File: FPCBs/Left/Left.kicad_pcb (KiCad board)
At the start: 2 copper layers, 20.8 x 40 mm, 7 parts, among them J1 Conn_01x02_Pin, SW1 SW_Rotary_1x6_MP

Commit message: Add connector
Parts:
- J1: footprint Connector_Coaxial:WR-MMCX_Wuerth_66012102111404_Vertical -> Leica-G9ii:FPC-2Rows-27Pins-0.23mm
- moved J1 57.2 mm to (147.1, 93.6), turned to 90 degrees
- moved R5 12.0 mm to (102.6, 98.0), turned to -108 degrees
- moved R1 12.0 mm to (114.4, 98.1), turned to 108 degrees
- moved R4 7.50 mm to (104.8, 94.9), turned to -144 degrees
- moved R2 7.40 mm to (112.2, 94.9), turned to 144 degrees
- moved R3 0.13 mm to (108.5, 93.7), turned to 180 degrees
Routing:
- net Net-(J1-Pin_2): track 27.5 -> 68.5 mm
- net Net-(J1-Pin_1): track 33.0 -> 38.9 mm
- net Net-(R3-Pad2): track 4.93 -> 4.28 mm
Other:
- board size 20.8 x 40 mm -> 47.4 x 14.5 mm

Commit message: Update to kicad 9
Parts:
- J1: value Conn_01x02_Pin -> To PCB; footprint Leica-G9ii:FPC-2Rows-27Pins-0.23mm -> Leica-G9ii:FPC-2Rows-27Pins-0.5mm

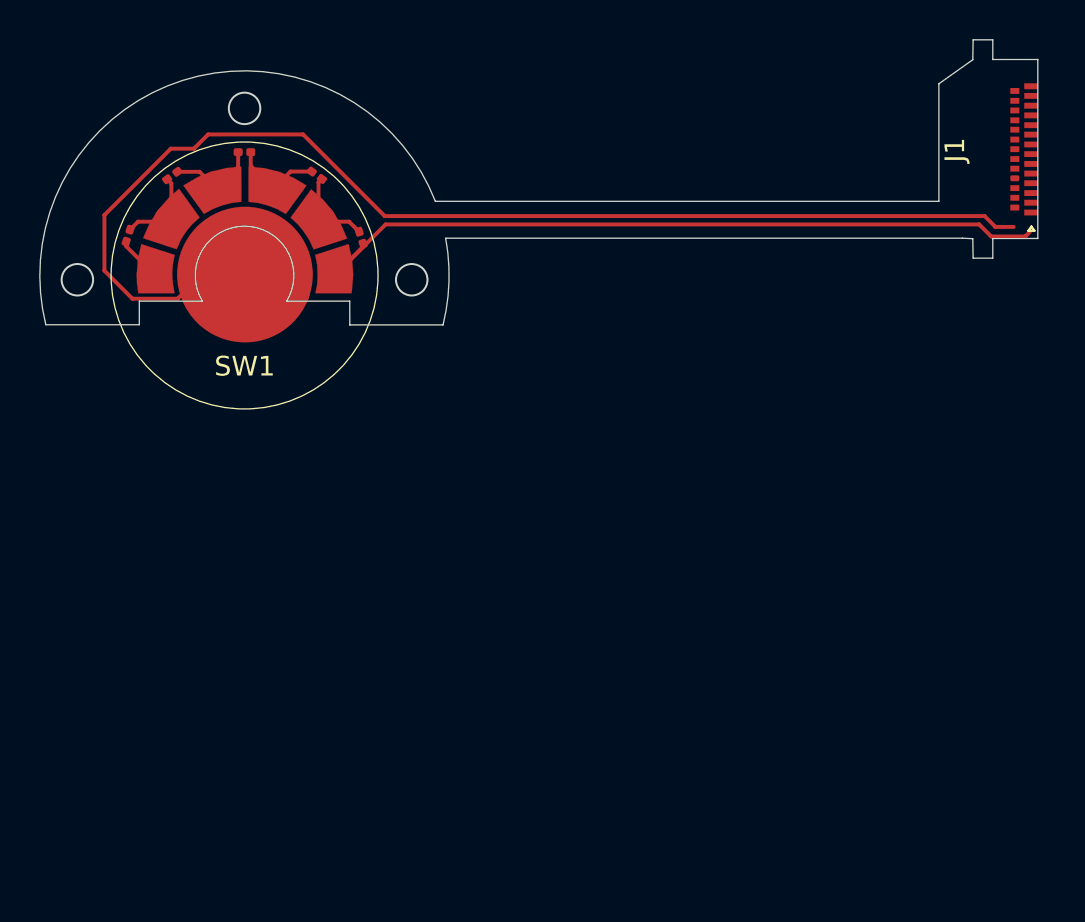
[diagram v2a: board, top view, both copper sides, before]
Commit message: Fixes on the left side FPC
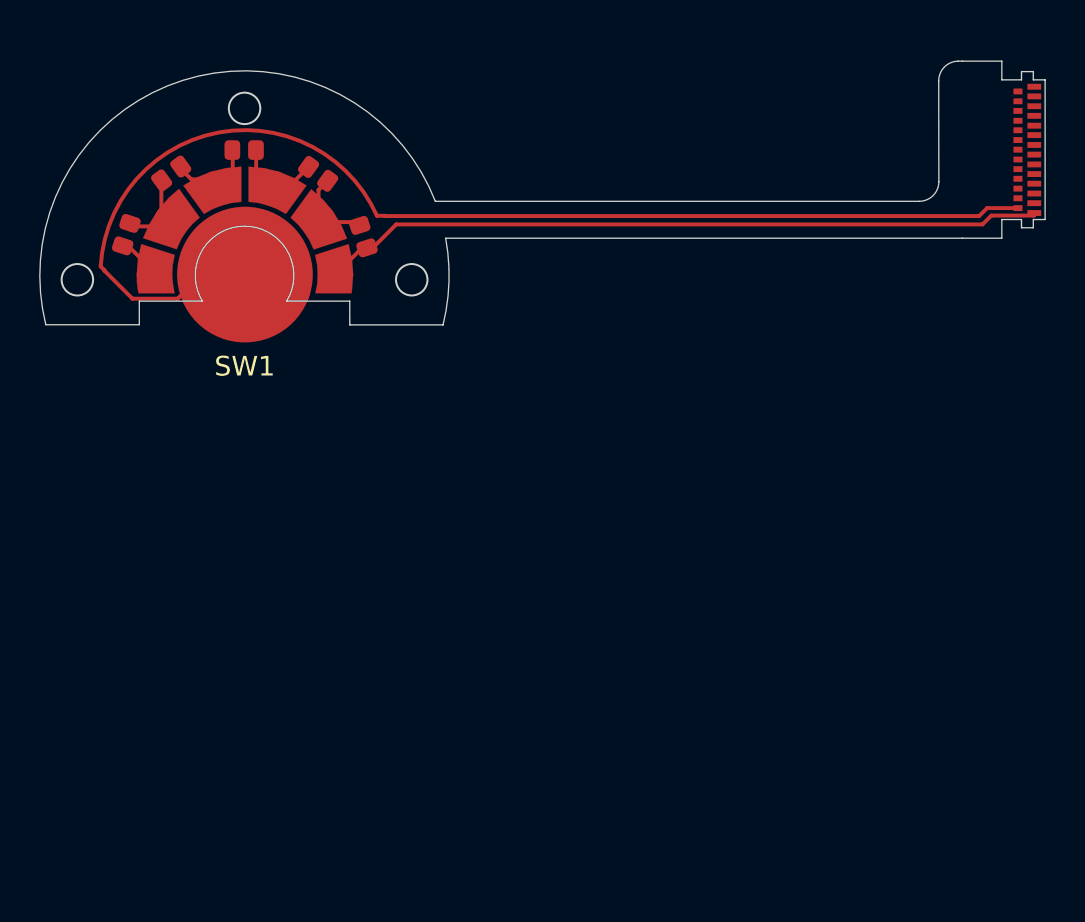
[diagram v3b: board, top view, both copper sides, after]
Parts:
- R1, R2, R3, R4, R5: footprint Resistor_SMD:R_0201_0603Metric -> Leica-G9ii:R_2x1mm
- moved J1 0.13 mm to (147.0, 93.6)
- moved R1 0.13 mm to (114.5, 98.0)
- moved R4 0.11 mm to (104.8, 94.8)
- moved R3 0.11 mm to (108.5, 93.6)
- moved R5 0.11 mm to (102.5, 97.9)
- moved R2 0.10 mm to (112.2, 94.8)
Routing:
- net Net-(J1-Pin_2): track 68.5 -> 48.8 mm
- net Net-(J1-Pin_1): track 38.9 -> 37.0 mm
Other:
- board size 47.4 x 14.5 mm -> 46.9 x 13.4 mm

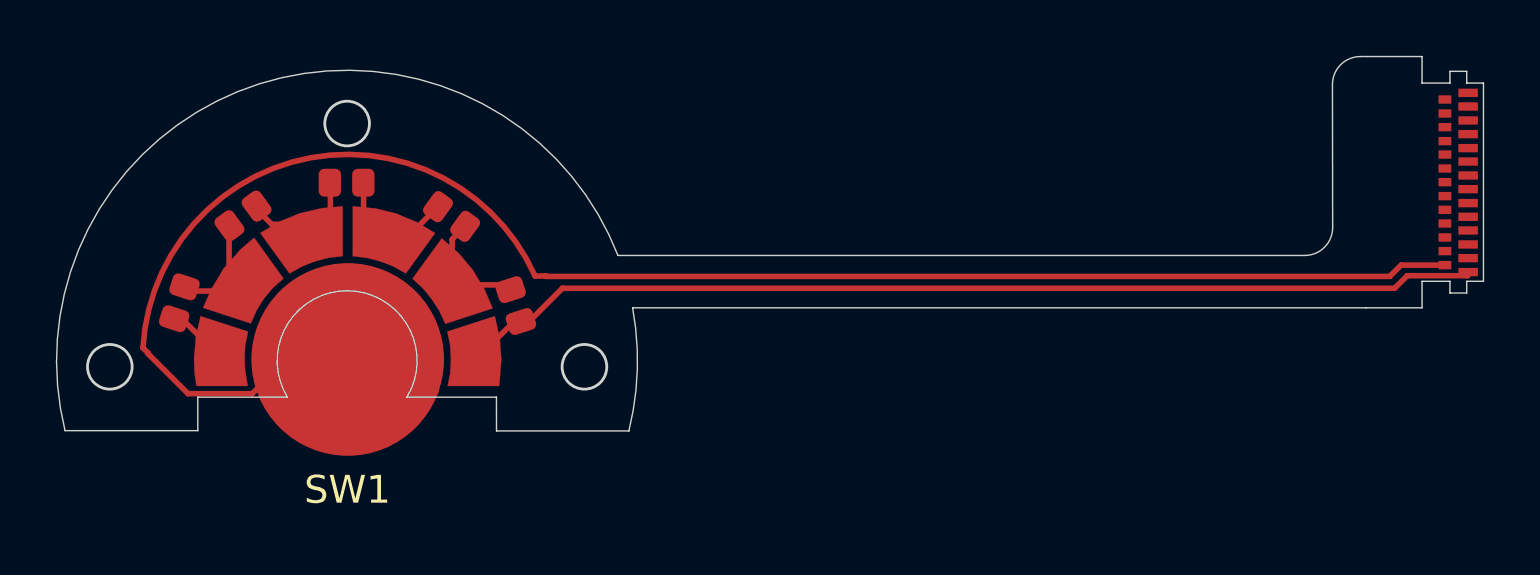
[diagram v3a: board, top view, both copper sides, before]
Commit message: Move leds to Right board
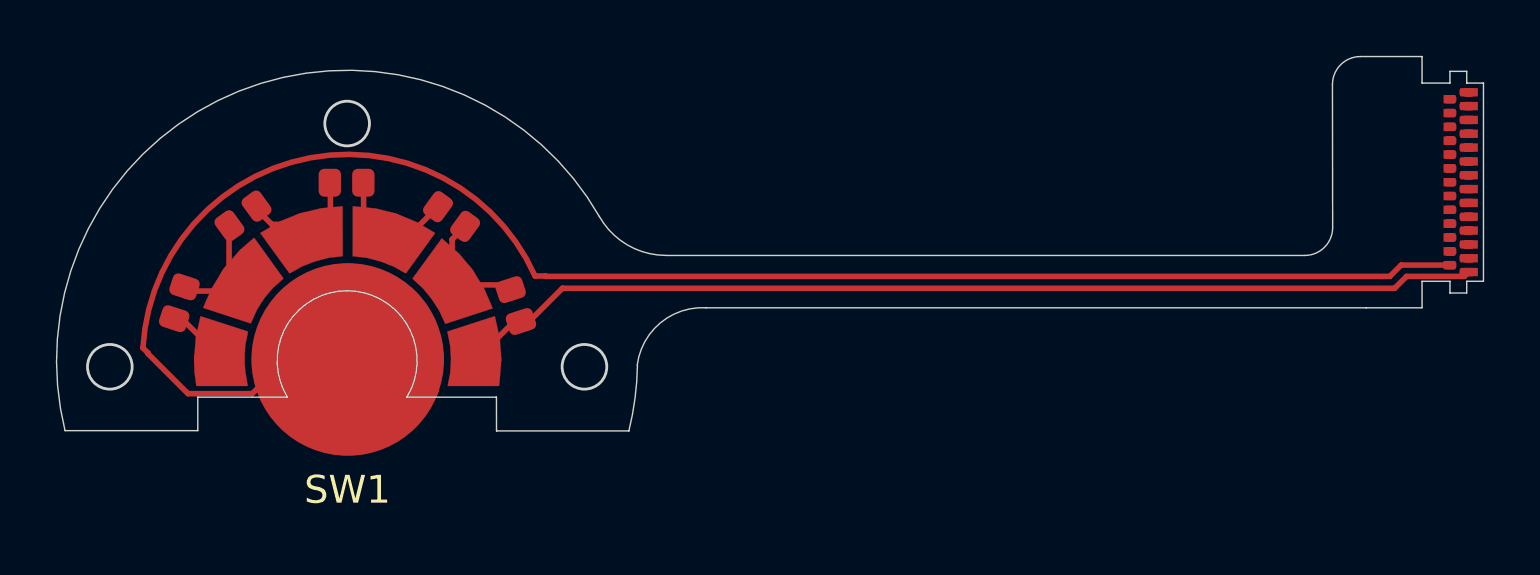
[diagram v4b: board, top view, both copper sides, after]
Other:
- outline, holes or cut-outs redrawn

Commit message: Add copper tot he back side
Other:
- outline, holes or cut-outs redrawn
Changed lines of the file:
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@@
 		(tenting front back)
 		(pcbplotparams
-			(layerselection 0x00000000_00000000_55f55555_5755f5ff)
+			(layerselection 0x00000000_00000000_55555555_5755f5ff)
 			(plot_on_all_layers_selection 0x00000000_00000000_00000000_00000000)
 			(disableapertmacros no)
@@
 			(usegerberattributes yes)
 			(usegerberadvancedattributes yes)
-			(creategerberjobfile yes)
+			(creategerberjobfile no)
 			(dashed_line_dash_ratio 12.000000)
 			(dashed_line_gap_ratio 3.000000)
@@
 			(sketchdnponfab yes)
 			(crossoutdnponfab yes)
-			(subtractmaskfromsilk no)
+			(subtractmaskfromsilk yes)
 			(outputformat 1)
 			(mirror no)
 			(drillshape 0)
 			(scaleselection 1)
-			(outputdirectory "export/drills/")
+			(outputdirectory "Gerber/")
 		)
 	)
@@
 	)
 	(gr_arc
-		(start 106.36 101.3)
-		(mid 108.5 97.488487)
-		(end 110.64 101.3)
+		(start 106.49 101.5)
+		(mid 108.380646 97.486841)
+		(end 110.643829 101.302335)
 		(stroke
 			(width 0.05)
@@
 	)
 	(gr_line
-		(start 103.15 101.3)
+		(start 103.15 101.5)
 		(end 103.15 102.5)
 		(stroke
@@
 	)
 	(gr_line
-		(start 106.36 101.3)
-		(end 103.15 101.3)
+		(start 106.49 101.5)
+		(end 103.15 101.5)
 		(stroke
 			(width 0.05)
-			(type default)
+			(type solid)
 		)
 		(layer "Edge.Cuts")

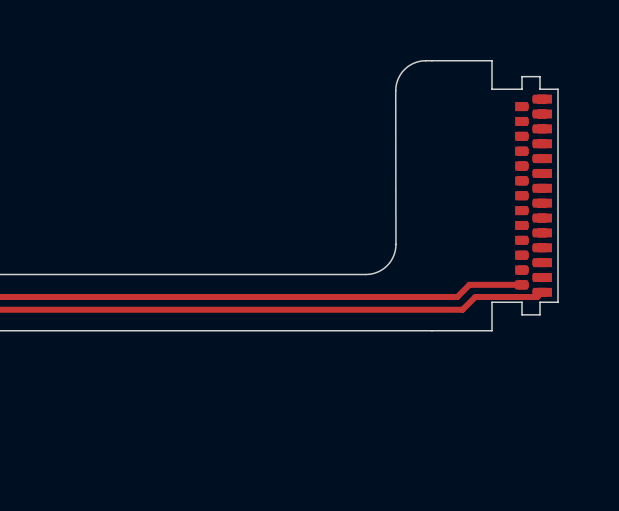
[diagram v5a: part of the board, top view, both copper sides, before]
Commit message: Add back copper
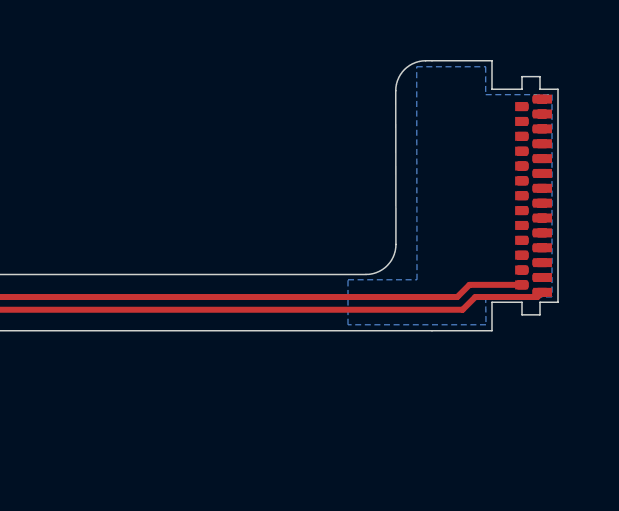
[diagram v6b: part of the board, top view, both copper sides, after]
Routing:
- added copper zone on B.Cu, net (none)
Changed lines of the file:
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@@
 		(net 7)
+	)
+	(zone
+		(net 0)
+		(net_name "")
+		(layer "B.Cu")
+		(hatch edge 0.5)
+		(connect_pads
+			(clearance 0.5)
+		)
+		(min_thickness 0.25)
+		(filled_areas_thickness no)
+		(fill yes
+			(thermal_gap 0.5)
+			(thermal_bridge_width 0.5)
+			(island_removal_mode 1)
+			(island_area_min 10)
+		)
+		(polygon
+			(pts
+				(xy 149 90.23) (xy 149 96.97) (xy 146.79 96.97) (xy 146.8 97.9) (xy 142.2 97.9) (xy 142.2 96.4)
+				(xy 144.5 96.4) (xy 144.49 89.3) (xy 146.79 89.3) (xy 146.79 90.23)
+			)
+		)
 	)
 	(embedded_fonts no)
